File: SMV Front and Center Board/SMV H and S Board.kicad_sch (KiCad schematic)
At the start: 43 parts, among them J1 XT60-M, J10 Molex Micro-Fit 4 Pin, J2 XT60-M, J3 XT60-M, J4 22035035, J7 22035035, J8 22035035, J9 22035035, Q1 PSMN1R8-40YLC_115 - MOSFET, Q3 PSMN1R8-40YLC_115 - MOSFET, U1 UA78M05QDCYRG4Q1, U3 PADS131M04QPWRQ1

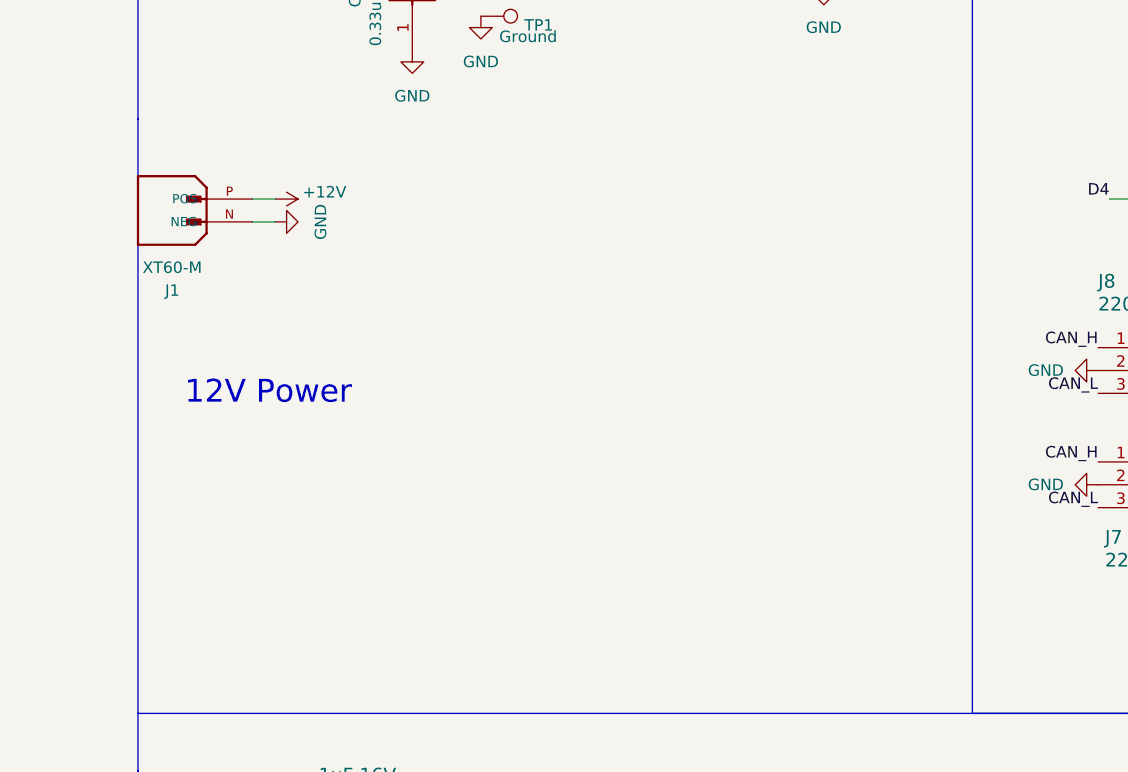
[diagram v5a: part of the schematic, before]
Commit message: Added 7.2V LDO for wipers
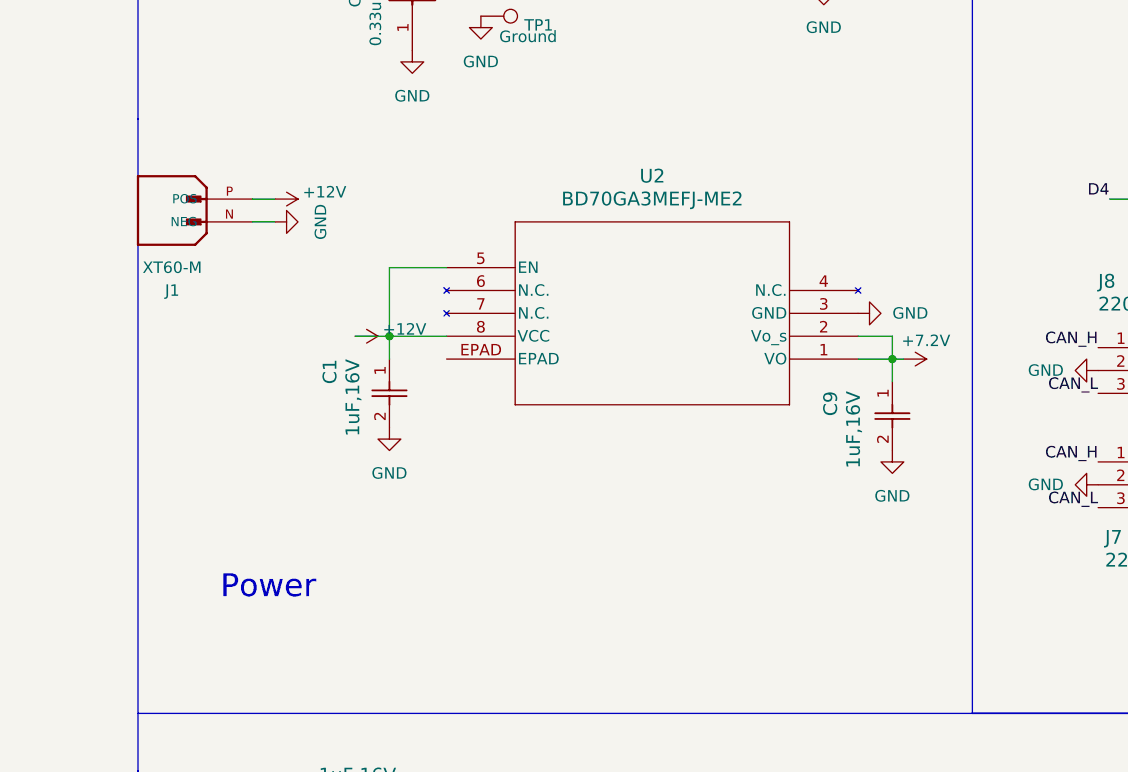
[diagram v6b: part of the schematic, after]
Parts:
- added C1, C9: 1uF,16V, SMV_Passives:Cap0805, symbol SMV_Custom:C0805C105K4RACTU
- added U2: BD70GA3MEFJ-ME2, SMV_ICs:HTSOP-J8_ROM, symbol SMV_Custom:BD70GA3MEFJ-ME2
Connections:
- net +12V: now also C1.1, U2.5 (EN), U2.8 (VCC)
- net +7.2V: now also C9.1, U2.1 (VO), U2.2 (Vo_s)
- net GND: now also C1.2, C9.2, U2.3 (GND)
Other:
- note added: "Power"
- note removed: "12V Power"

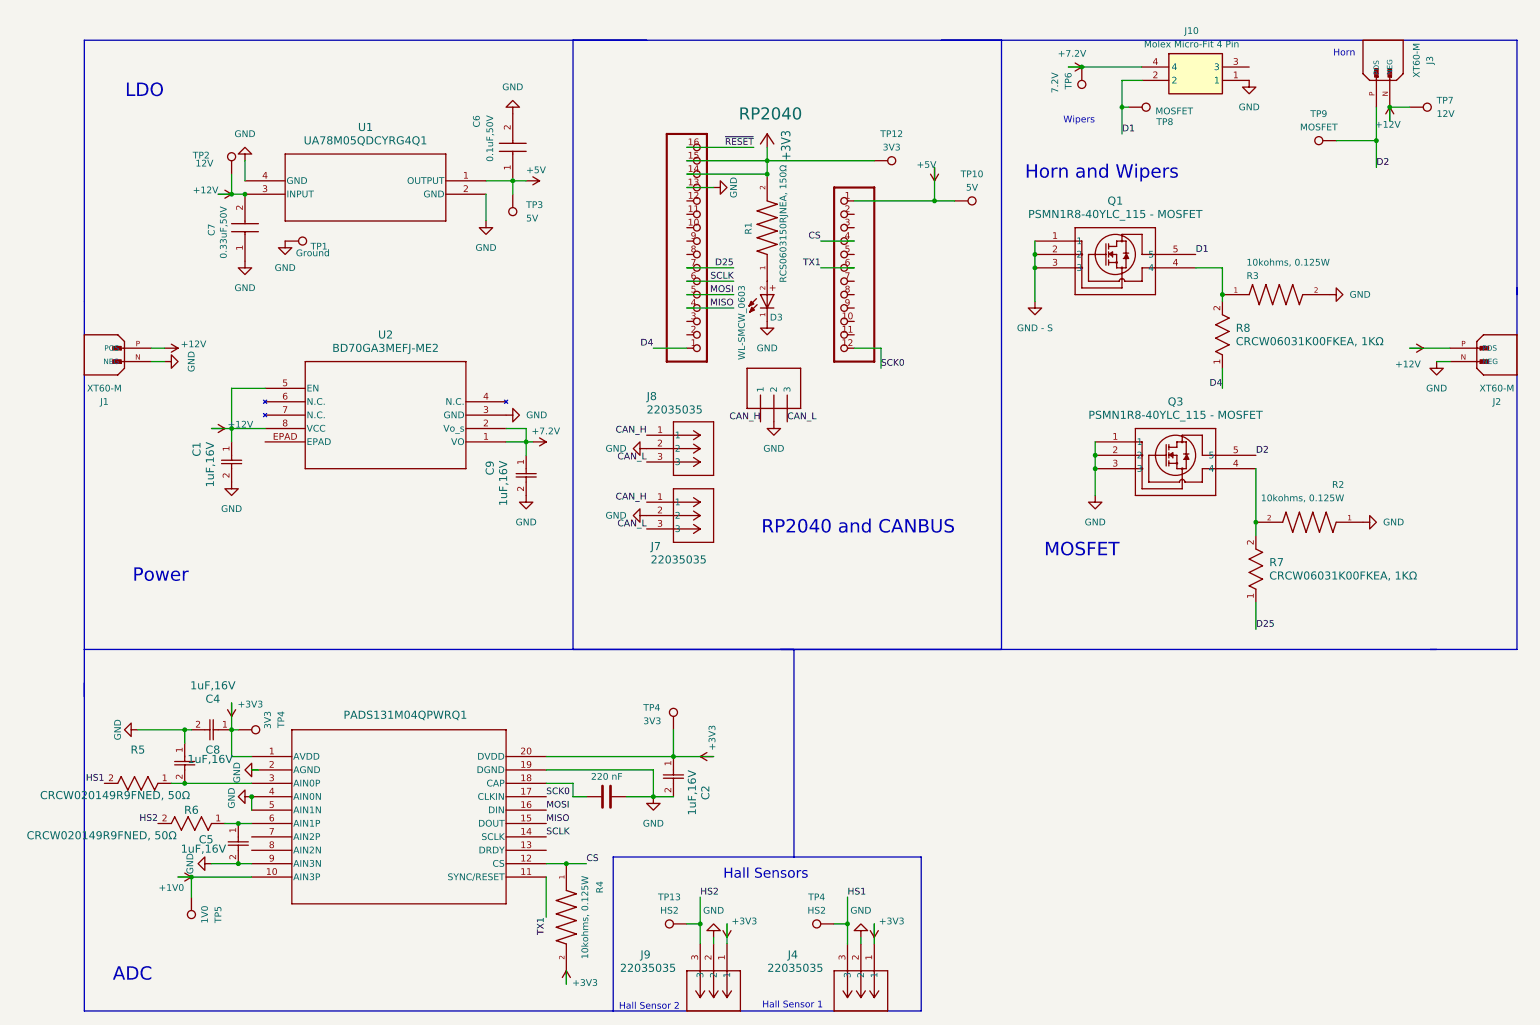
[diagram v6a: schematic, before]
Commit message: Fixed readability, added no-connect flags, reoriented grounds
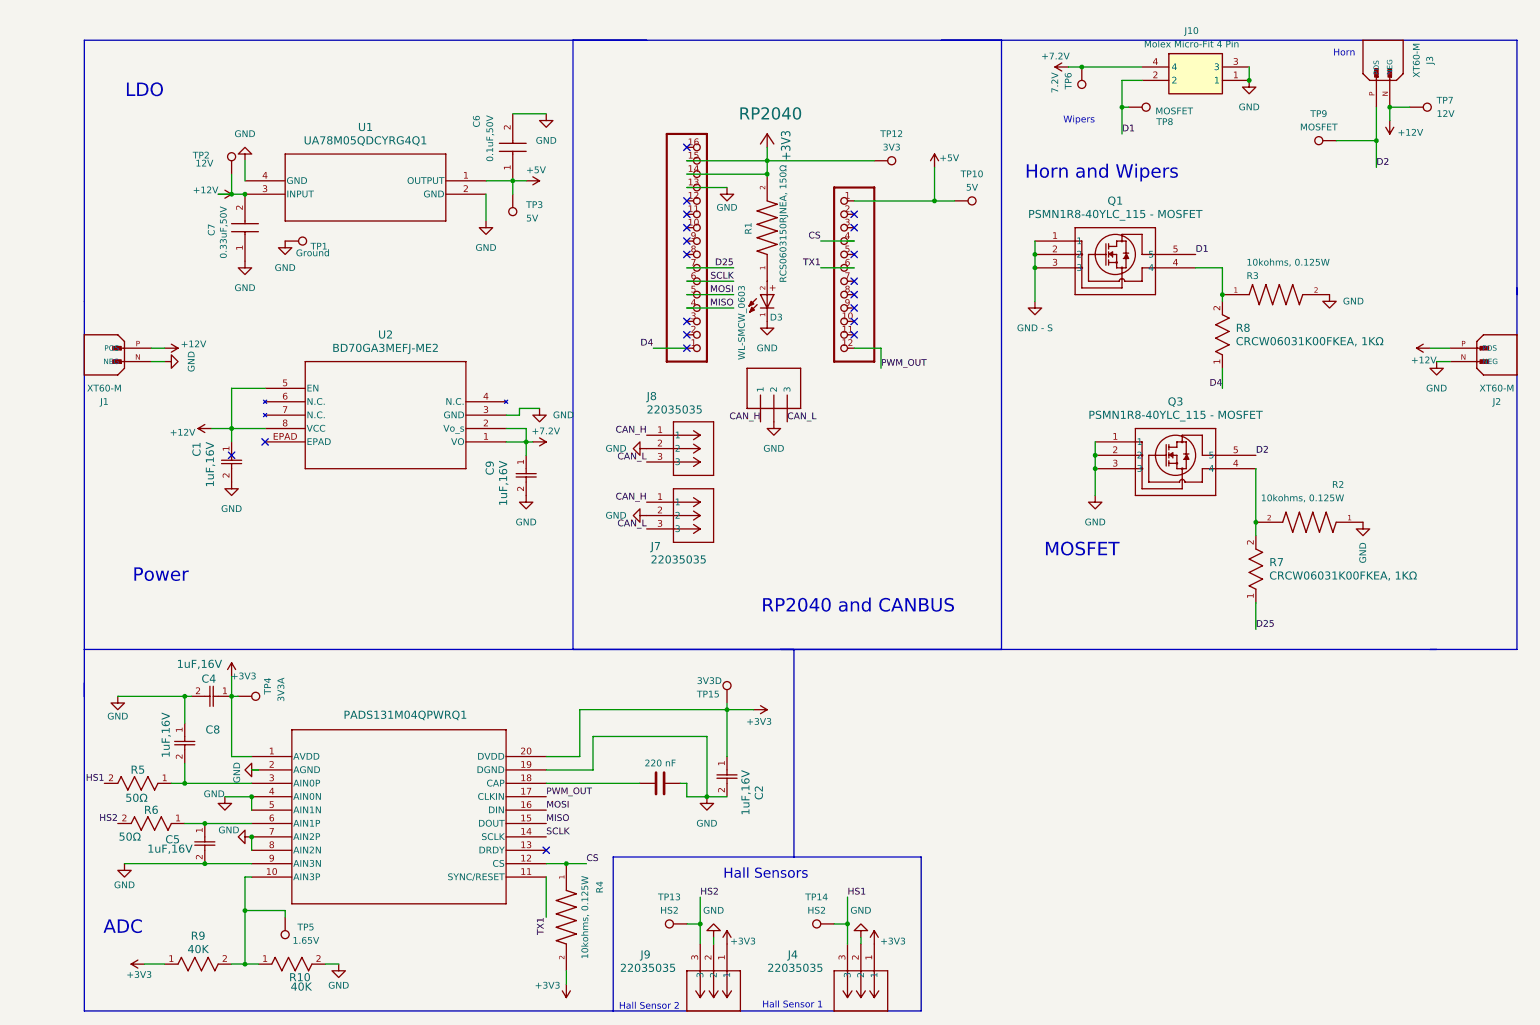
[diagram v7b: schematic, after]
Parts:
- added R10, R9: 40K, SMV_Passives:0805RESC2012X60N, symbol SMV_Custom:CRCW080540K0FKEA
- R5, R6: value CRCW020149R9FNED, 50Ω -> 50Ω
- TP15: renamed from 3V3; value TP4 -> 3V3D
- TP4: renamed from 3V3; value TP4 -> 3V3A
- TP5: value 1V0 -> 1.65V
- renumbered TP4 to TP14
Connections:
- net SCK0 is gone; now on net PWM_OUT: RP2040.12, U3.17 (CLKIN)
- net +3V3: now also R9.1
- net GND: now also J10.3, U3.7 (AIN2P), U3.8 (AIN2N), R10.2
- net PWM_OUT: now reaches RP2040.12
- net +1V0: no longer names the net of TP5.1, U3.10 (AIN3P)
- net +1V0: now also R10.1, R9.2
- net ~{RESET}: no longer names the net of RP2040.16
- no-connect marks 0 -> 20
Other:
- moved on the sheet: C2, C4, C5, C8, R6, TP15, TP4, TP5

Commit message: Implemented final checks
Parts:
- removed C1, C9: 1uF,16V, SMV_Passives:Cap0805, symbol SMV_Custom:C0805C105K4RACTU
- removed J1, J2: XT60-M, XT60-M:AMASS_XT60-M, symbol XT60-M:XT60-M
- removed U2: BD70GA3MEFJ-ME2, SMV_ICs:HTSOP-J8_ROM, symbol SMV_Custom:BD70GA3MEFJ-ME2
- added D1, D2: WL-SMCW_0603, SMV_Passives:WL-SMCW_0603(diode), symbol SMV_Custom:WL-SMCW_0603
- added J1, J2: 430450200, SMV_Connectors:CONN_SD-43045-001_02_MOL, symbol SMV_Custom:430450200
- added R11, R12: 150Ω, SMV_Passives:0805RESC2012X60N, symbol SMV_Custom:RCS0603150RJNEA
- added R13, R14, R15, R16: 10kohms, 0.125W, SMV_Passives:0805RESC2012X60N, symbol SMV_Custom:CRCW080510K0FKEAC
- added TP11, TP16: TestPoint, symbol Connector:TestPoint
- C7: value 0.33uF,50V -> 0.47uF,50V
- TP14: value HS2 -> HS1
- TP6: value 7.2V -> 12V
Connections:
- net +7.2V is gone; now on net +12V: J10.4, TP6.1
- net +12V: now also J2.1
- net +3V3: no longer J4.1, J9.1
- net GND: now also D1.1, J2.2, R14.2, R16.2
- net HS1: now also R15.1, R16.1; no longer J4.3, TP14.1
- net HS2: now also R13.2, R14.1; no longer J9.3, TP13.1
- net MISO: now also TP16.1
- net MOSI: now also TP11.1
- net at RP2040.11: now also R12.2
- new net: J9.3, R13.1, TP13.1
- new net: J4.3, R15.2, TP14.1
- new net: R11.2, RP2040.12
- new net: D2.2, R12.1
- new net: D1.2, R11.1
- new net +3.3V: J4.1, J9.1
- no-connect marks 20 -> 16
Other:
- note added: "Gas"
- note removed: "Hall Sensors"
- moved on the sheet: J4, TP14
